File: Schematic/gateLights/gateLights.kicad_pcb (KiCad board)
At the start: 2 copper layers, 110 x 100 mm, 25 parts, among them J1 CONN_01X06, J2 CONN_02X03, J3 CONN_01X02, U1 OPTO-TRIAC MOC302x, U2 OPTO-TRIAC MOC302x, U3 OPTO-TRIAC MOC302x, U4 OPTO-TRIAC MOC302x, U5 OPTO-TRIAC MOC302x, U6 ATTINY1634-SU, U7 MC33063A

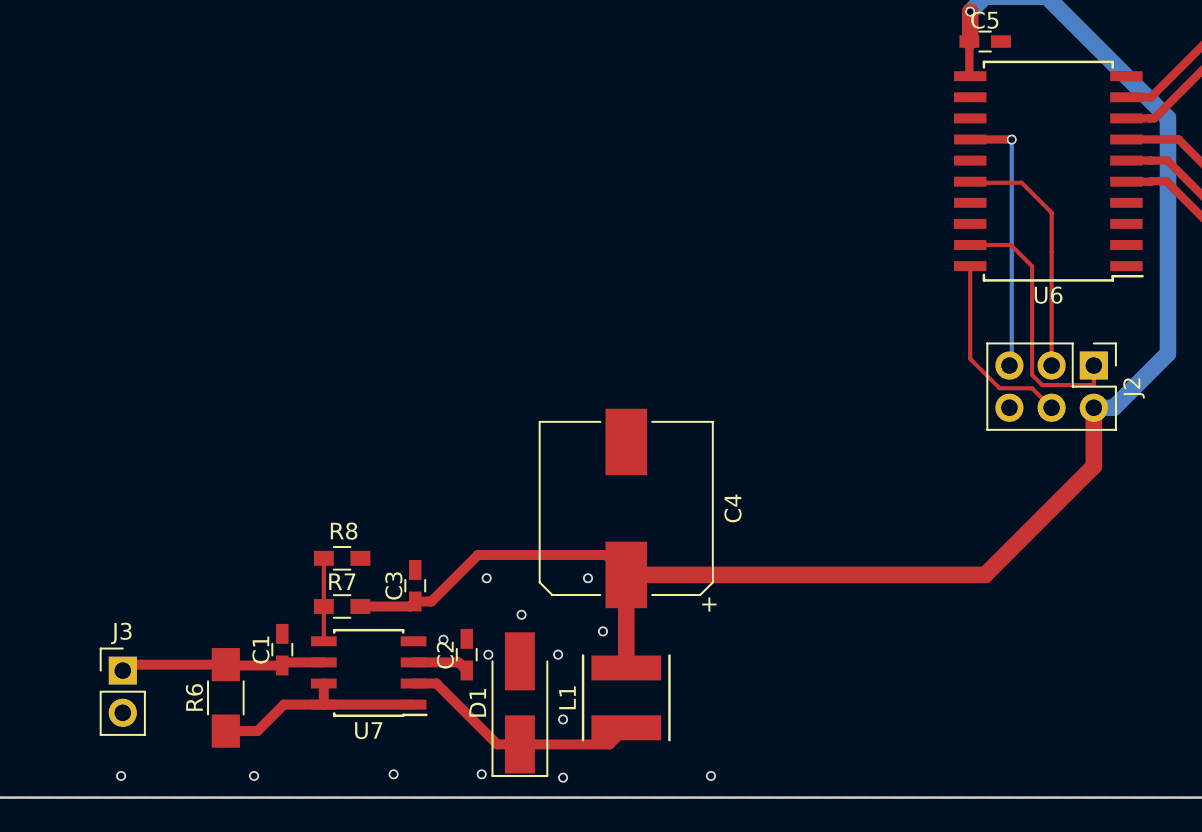
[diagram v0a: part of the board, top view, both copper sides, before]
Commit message: RS485 protection
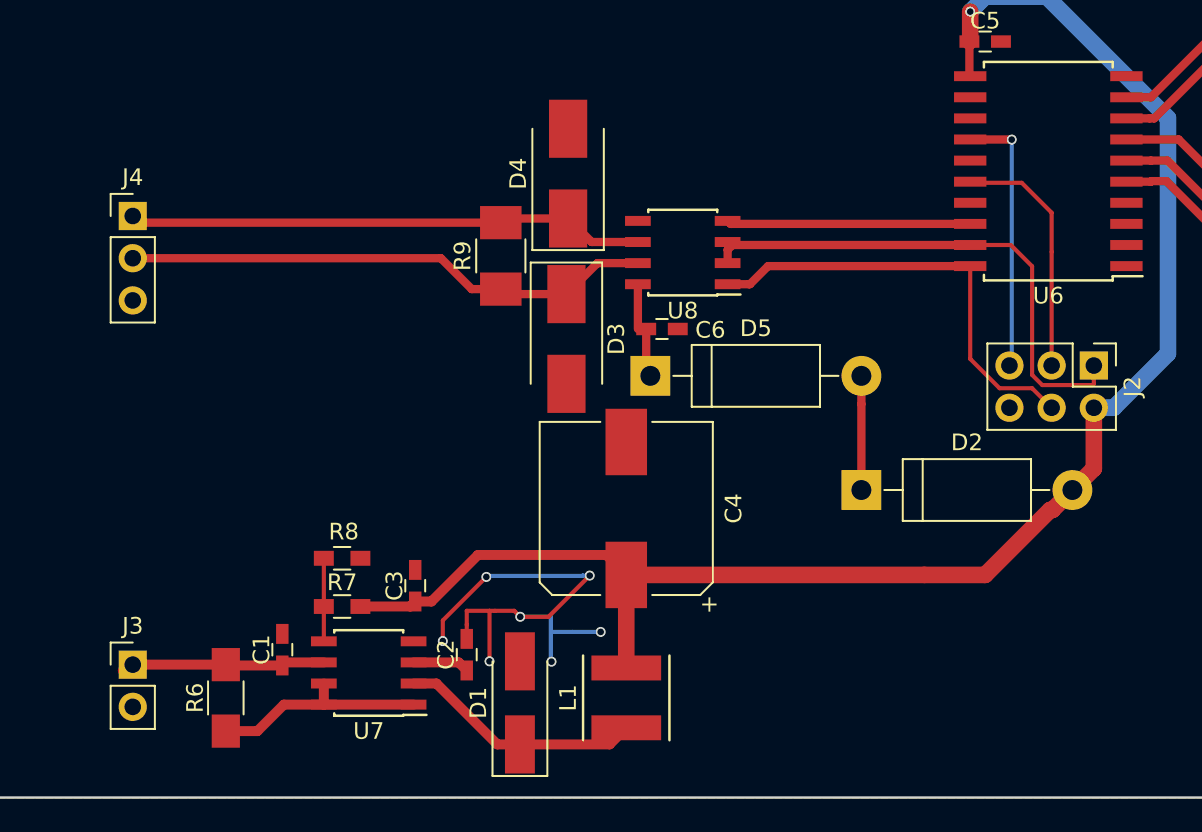
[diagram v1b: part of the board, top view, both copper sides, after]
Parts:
- added C6: 100nF, Capacitors_SMD:C_0603_HandSoldering, F.Cu at (96.8, 111.8)
- added D2: 2N4001, Diodes_THT:D_DO-15_P12.70mm_Horizontal, F.Cu at (108.8, 121.5)
- added D3: SMBJ5.0, Diodes_SMD:D_SMB_Handsoldering, F.Cu at (91.1, 112.4)
- added D4: SMBJ5.0, Diodes_SMD:D_SMB_Handsoldering, F.Cu at (91.2, 102.5)
- added D5: 2N4001, Diodes_THT:D_DO-15_P12.70mm_Horizontal, F.Cu at (96.2, 114.6)
- added J4: CONN_01X03, Pin_Headers:Pin_Header_Straight_1x03_Pitch2.54mm, F.Cu at (65.0, 105.0)
- added R9: 240R, Resistors_SMD:R_1210_HandSoldering, F.Cu at (87.2, 107.4)
- added U8: SP3485CN, Housings_SOIC:SOIC-8_3.9x4.9mm_Pitch1.27mm, F.Cu at (98.1, 107.2)
- moved J3 0.70 mm to (65.0, 132.0)
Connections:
- net /Processor/MISO renamed /RS485/DE
- net /Processor/MOSI renamed /RS485/DO
- net Net-(U6-Pad1) renamed /Processor/UART0_TX
- net Net-(U6-Pad2) renamed /Processor/UART0_RX
- U6 pad 18: Net-(U6-Pad18) -> /RS485/DI
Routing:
- net GND: track 0.00 -> 32.3 mm, vias 0 -> 7
- net /RS485/RS485_B: track 0.00 -> 32.1 mm
- net /RS485/RS485_A: track 0.00 -> 31.3 mm
- net /RS485/DE: track 15.9 -> 31.4 mm
- net /RS485/DO: track 11.7 -> 26.8 mm
- net /RS485/DI: track 0.00 -> 14.7 mm
- net Net-(D2-Pad1): track 0.00 -> 6.87 mm
- net Net-(C6-Pad1): track 0.00 -> 5.62 mm
- net (no net): track 0.33 -> 0.00 mm, vias 14 -> 0

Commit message: Add inputs
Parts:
- added J5: CONN_01X04, Pin_Headers:Pin_Header_Straight_1x04_Pitch2.54mm, F.Cu at (65.8, 92.8)
- added Q1: 2N7002, TO_SOT_Packages_SMD:SOT-23, F.Cu at (101.5, 92.7)
- added Q2: 2N7002, TO_SOT_Packages_SMD:SOT-23, F.Cu at (101.5, 87.8)
- added Q3: 2N7002, TO_SOT_Packages_SMD:SOT-23, F.Cu at (101.5, 82.7)
- added R10: 27K, Resistors_SMD:R_1210_HandSoldering, F.Cu at (88.0, 92.0)
- added R11: 10K, Resistors_SMD:R_1210_HandSoldering, F.Cu at (95.1, 91.8)
- added R12: 27K, Resistors_SMD:R_1210_HandSoldering, F.Cu at (88.0, 87.0)
- added R13: 10K, Resistors_SMD:R_1210_HandSoldering, F.Cu at (95.1, 86.9)
- added R14: 10K, Resistors_SMD:R_1210_HandSoldering, F.Cu at (106.6, 92.9)
- added R15: 10K, Resistors_SMD:R_1210_HandSoldering, F.Cu at (106.6, 85.9)
- added R16: 27K, Resistors_SMD:R_1210_HandSoldering, F.Cu at (88.0, 81.9)
- added R17: 10K, Resistors_SMD:R_1210_HandSoldering, F.Cu at (95.1, 81.8)
- added R18: 10K, Resistors_SMD:R_1210_HandSoldering, F.Cu at (106.6, 78.7)
- L1: footprint Inductors:Inductor_Taiyo-Yuden_MD-5050 -> GateLight:SCD1005
- moved C4 23.6 mm to (116.4, 131.9), turned to 270 degrees
- moved L1 6.32 mm to (100.4, 131.3), turned to 180 degrees
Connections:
- net /Processor/SCK renamed /Processor/IN_2
- U6 pad 15: Net-(U6-Pad15) -> /Processor/IN_3
- U6 pad 17: Net-(U6-Pad17) -> /Processor/IN_1
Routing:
- net Net-(Q1-Pad1): track 0.00 -> 12.4 mm
- net Net-(Q3-Pad1): track 0.00 -> 12.4 mm
- net Net-(Q2-Pad1): track 0.00 -> 12.3 mm
- net Net-(D1-Pad1): track 14.7 -> 23.2 mm
- net /Processor/IN_3: track 0.00 -> 5.69 mm
- net /Processor/IN_1: track 0.00 -> 5.62 mm
- net /Processor/IN_2: track 14.9 -> 19.0 mm
- net +5V: track 97.0 -> 99.4 mm

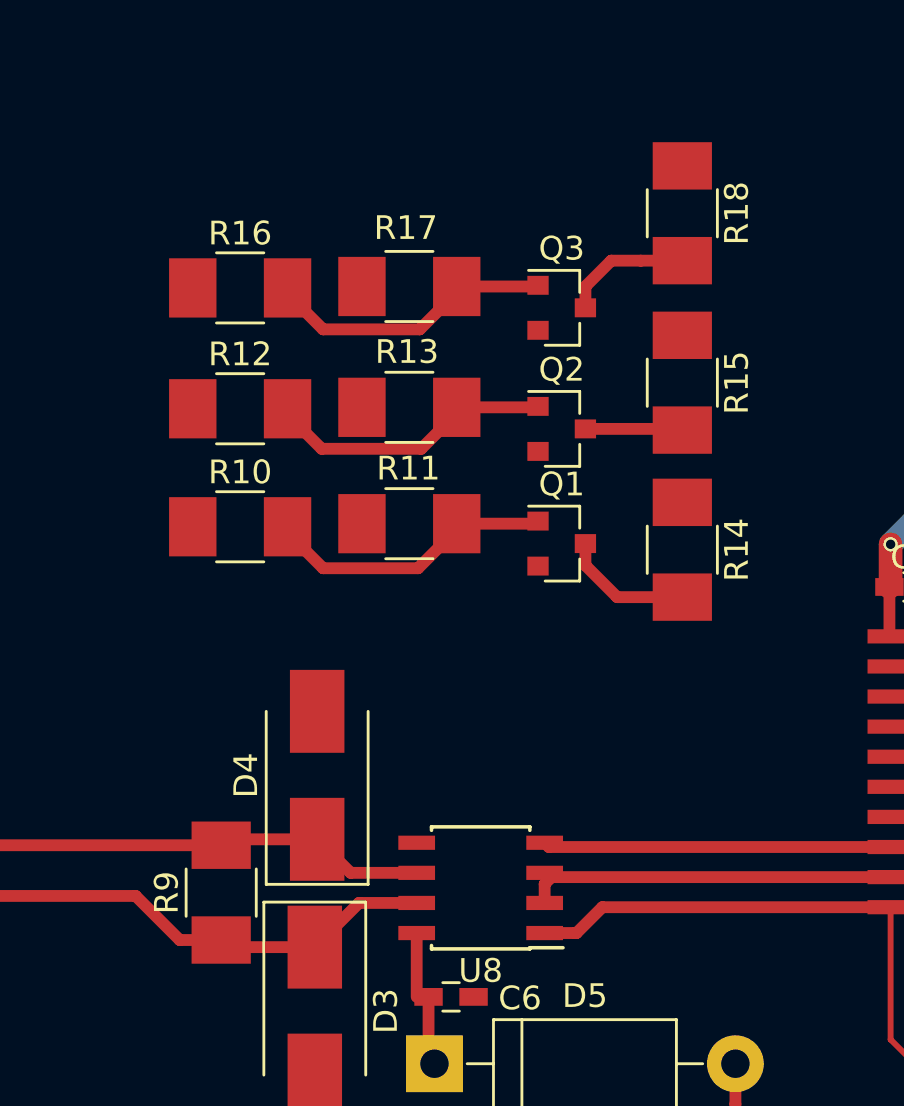
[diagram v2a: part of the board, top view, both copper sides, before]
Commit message: Fix resistor footprints
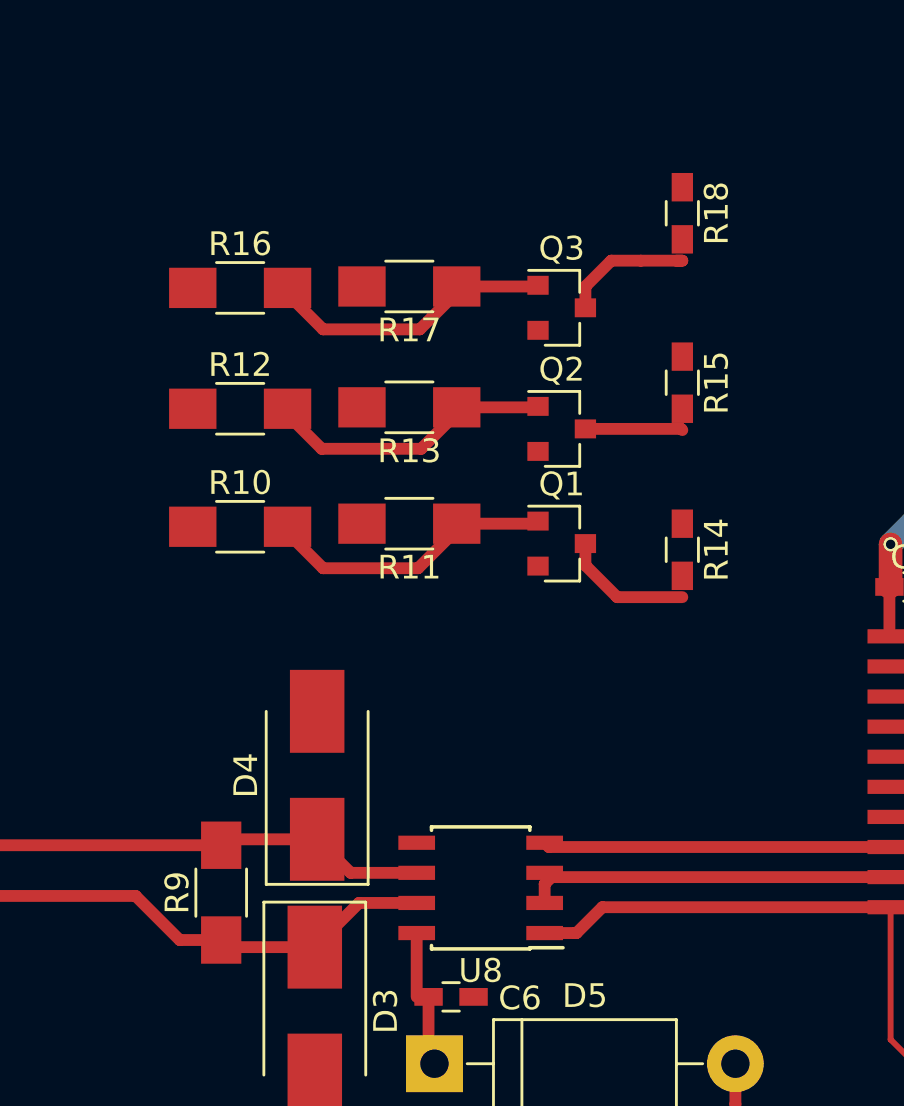
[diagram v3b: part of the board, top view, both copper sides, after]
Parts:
- R10, R11, R12, R13, R16, R17, R9: footprint Resistors_SMD:R_1210_HandSoldering -> Resistors_SMD:R_1206_HandSoldering
- R14, R15, R18: footprint Resistors_SMD:R_1210_HandSoldering -> Resistors_SMD:R_0603_HandSoldering
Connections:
- J2 pad 1: /RS485/DE -> /RS485/DI
- U6 pad 18: /RS485/DI -> /RS485/DE
- U6 pad 19: /RS485/DE -> /RS485/DI
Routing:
- net /RS485/DE: track 31.4 -> 15.5 mm
- net /RS485/DI: track 14.7 -> 30.6 mm
